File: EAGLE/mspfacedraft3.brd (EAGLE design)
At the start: 70.1 x 70.1 mm, 26 parts, among them M1 G1040003D_LRA, P1 POT

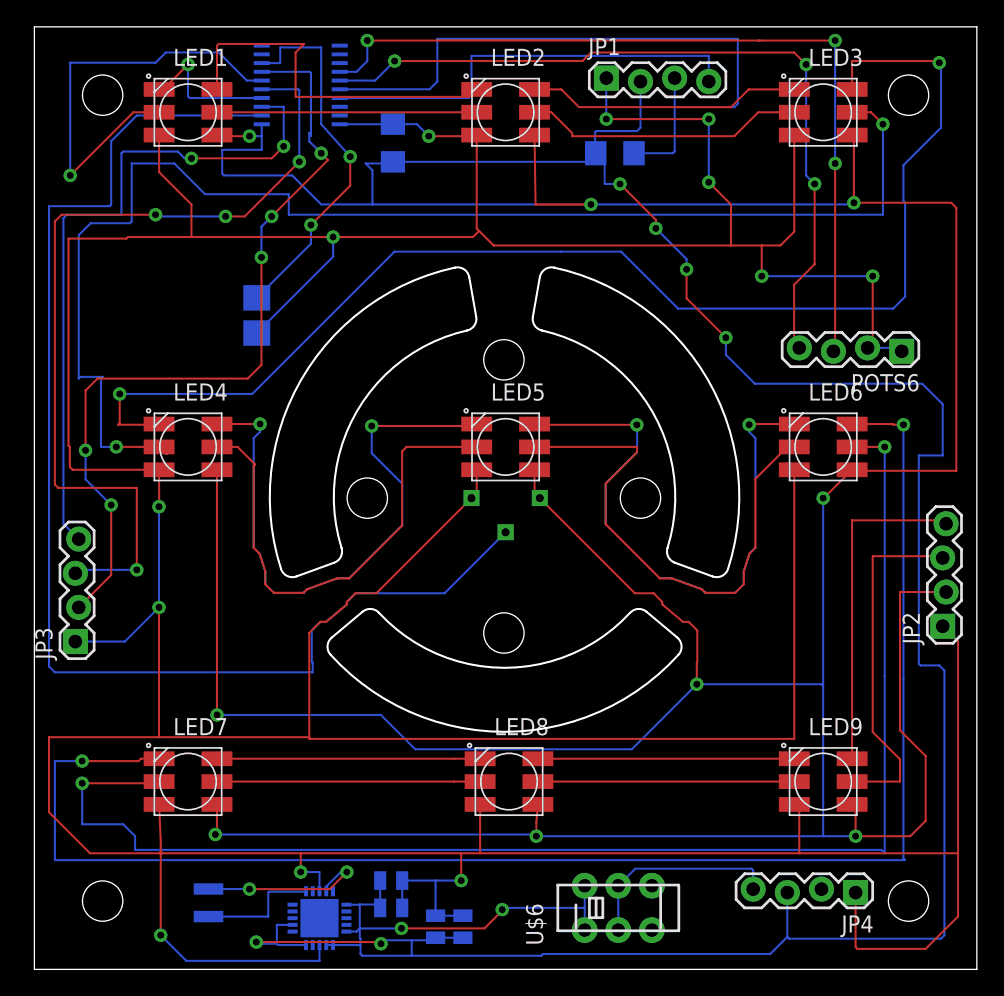
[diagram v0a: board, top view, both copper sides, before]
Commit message: added msp face v3 pcb
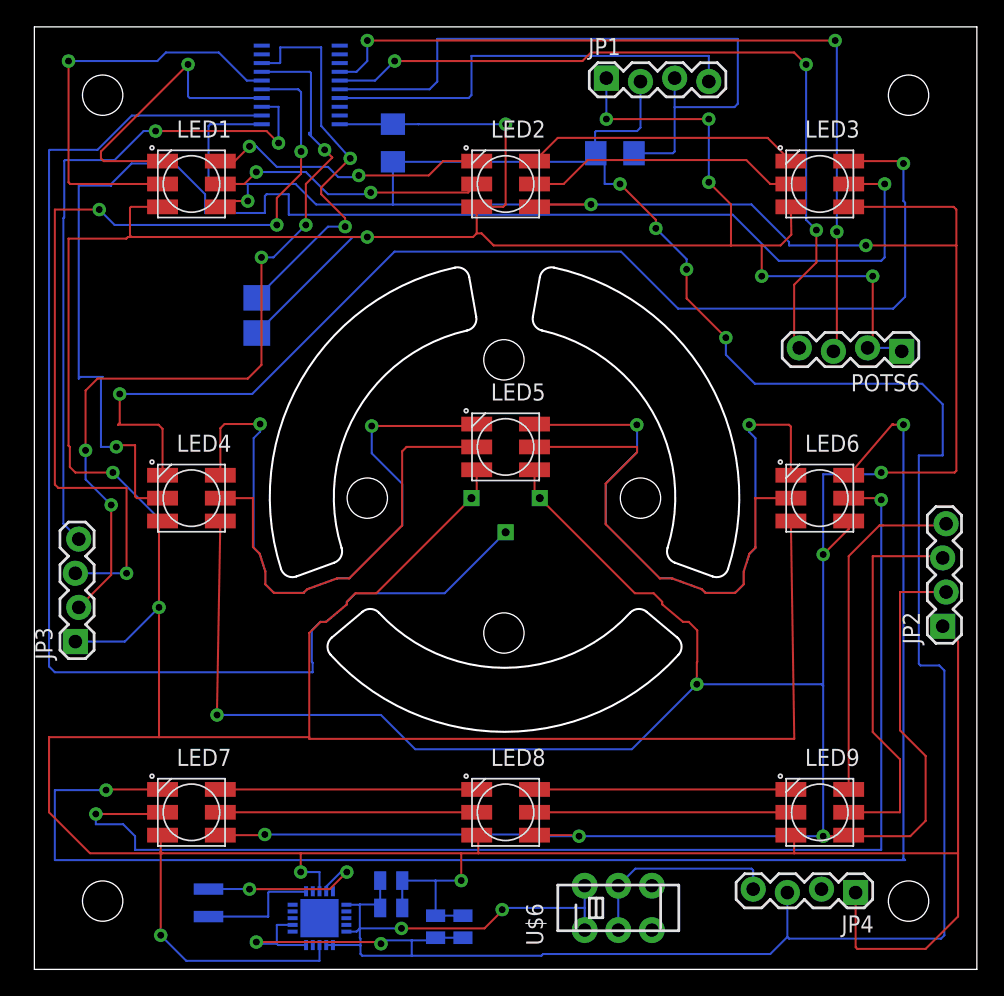
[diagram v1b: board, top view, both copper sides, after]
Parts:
- moved LED1 5.34 mm to (11.7, 58.4)
- moved LED3 5.34 mm to (58.4, 58.4)
- moved LED2 5.33 mm to (35.1, 58.4)
- moved LED4 3.82 mm to (11.7, 35.1)
- moved LED6 3.82 mm to (58.4, 35.1)
- moved LED7 2.30 mm to (11.7, 11.7)
- moved LED8 2.30 mm to (35.1, 11.7)
- moved LED9 2.30 mm to (58.4, 11.7)
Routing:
- net N$7: track 10.8 -> 22.2 mm
- net N$5: track 97.7 -> 88.3 mm
- net GND: track 448.0 -> 438.7 mm
- net N$14: track 102.7 -> 94.1 mm
- net N$1: track 27.7 -> 21.0 mm, vias 0 -> 2
- net N$6: track 100.2 -> 105.5 mm
- net VCC: track 518.7 -> 515.0 mm, vias 17 -> 18
- net N$10: track 36.1 -> 32.6 mm
- net N$11: track 44.2 -> 47.6 mm
- net N$9: track 44.1 -> 47.5 mm
- net N$12: track 38.8 -> 36.2 mm
- net OUT2: track 27.4 -> 30.0 mm
- net P2.0: track 27.9 -> 30.1 mm
- net POT3: track 64.8 -> 66.7 mm
- net N$2: track 19.3 -> 20.4 mm, vias 0 -> 2
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
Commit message: Schematic/brd updates/fixes
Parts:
- removed JP3, JP4, POTS6: (no value), SparkFun:1X04_LOCK
- added BATT: M02, mspfacedraft3:2PINHEADER
- added POTS: M06, mspfacedraft3:6PINHEADER
- moved C1 2.36 mm to (28.4, 5.97), turned to 270 degrees
- moved C3 2.05 mm to (31.8, 2.41)
- moved C4 2.05 mm to (33.8, 2.41)
- moved C2 0.65 mm to (26.4, 5.97), turned to 270 degrees
- renumbered JP1 to PROGRAM, JP2 to LEDOUT, M1 to HAPTIC, U$1 to MSP430, U$6 to SWITCH
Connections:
- net N$20 renamed POT1
- net N$7 renamed DI
- net N$8 renamed CI
- removed net P2.1: MSP430.9
- new net VBAT: C1.2, C2.2, LED10.10, LED10.11, LED10.12, LED10.6, LED10.7, LED10.8, LED10.9, SWITCH.1, SWITCH.4
- net GND: now also BATT.1, POTS.1; no longer JP3.1, JP4.1, POTS6.1, POTS6.2
- net POT2: now also POTS.6; no longer JP3.4
- net POT3: now also POTS.5; no longer JP3.3
- net POT4: now also POTS.4; no longer JP3.2
- net POT5: now also POTS.3; no longer POTS6.3
- net POT6: now also POTS.2; no longer POTS6.4
- net VCC: now also LED10.18, LED10.19, LED10.20; no longer C1.2, C2.2, JP4.3, LED10.10, LED10.11, LED10.12, LED10.6, SWITCH.1, SWITCH.4
- net VINBAT: now also BATT.2; no longer JP4.4
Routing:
- net VCC: track 515.0 -> 470.1 mm, vias 18 -> 16
- net VBAT: track 0.00 -> 26.1 mm
- net POT6: track 58.2 -> 78.6 mm, vias 3 -> 1
- net CI: track 31.6 -> 16.5 mm
- net GND: track 438.7 -> 424.8 mm, vias 12 -> 10
- net DI: track 22.2 -> 12.7 mm
- net POT3: track 66.7 -> 60.6 mm, vias 4 -> 3
- net POT5: track 62.0 -> 67.5 mm, vias 3 -> 1
- net POT4: track 61.1 -> 63.3 mm
- net N$6: track 105.5 -> 103.6 mm
- net POT1: track 95.7 -> 94.2 mm
- net VINBAT: track 15.3 -> 14.1 mm
- net POT2: track 49.8 -> 50.8 mm
- net N$21: track 9.08 -> 8.17 mm
- net N$19: track 13.1 -> 12.3 mm, vias 2 -> 0
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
